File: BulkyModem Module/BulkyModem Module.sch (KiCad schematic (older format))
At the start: 12 parts, among them M1 Mounting, M2 Mounting, M3 Mounting, M4 Mounting, U1 74HCT244

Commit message: Initial layout
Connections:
- net ESP_RI: now reaches A1.23 (D5)
- no-connect marks 15 -> 14
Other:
- note added: "Note that the DCD/RI signal is shared between the two, something I'll\n"probably" get away with since they are only outgoing signals. The\n232 side will get buffered by the inverter used."
- note removed: "Note that the DCD signal is shared between the two, something I'll\n"probably" get away with since they are only outgoing signals. The\n232 side will get buffered by the inverter used."
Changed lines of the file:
@@
 NoConn ~ 8650 3825
 NoConn ~ 8650 3725
-NoConn ~ 8650 3625
 NoConn ~ 8650 3225
 NoConn ~ 8650 2925
@@
 	8650 3125 8875 3125
 $Sheet
-S 1925 1800 1025 700
+S 1925 1575 1025 825
 U 6379233A
 F0 "RS-232" 50
 F1 "rs232.sch" 50
-F2 "232_TX" I L 1925 2000 50
-F3 "232_RX" O L 1925 2100 50
-F4 "232_CTS" O L 1925 2300 50
-F5 "232_RTS" I L 1925 2200 50
-F6 "232_DCD" I L 1925 2400 50
+F2 "232_TX" I L 1925 1775 50
+F3 "232_RX" O L 1925 1875 50
+F4 "232_CTS" O L 1925 2075 50
+F5 "232_RTS" I L 1925 1975 50
+F6 "232_DCD" I L 1925 2175 50
+F7 "232_RI" I L 1925 2275 50
 $EndSheet
 $Sheet
@@
 	2425 3600 2500 3600
 Wire Wire Line
-	1925 2000 1400 2000
-Wire Wire Line
-	1400 2100 1925 2100
-Wire Wire Line
-	1925 2200 1400 2200
-Wire Wire Line
-	1400 2300 1925 2300
-Text Label 1425 2000 0    50   ~ 0
+	1925 1775 1400 1775
+Wire Wire Line
+	1400 1875 1925 1875
+Wire Wire Line
+	1925 1975 1400 1975
+Wire Wire Line
+	1400 2075 1925 2075
+Text Label 1425 1775 0    50   ~ 0
 232_TX
-Text Label 1425 2100 0    50   ~ 0
+Text Label 1425 1875 0    50   ~ 0
 232_RX
-Text Label 1425 2200 0    50   ~ 0
+Text Label 1425 1975 0    50   ~ 0
 232_RTS
-Text Label 1425 2300 0    50   ~ 0
+Text Label 1425 2075 0    50   ~ 0
 232_CTS
 Entry Wire Line
-	1400 2000 1300 2100
-Entry Wire Line
-	1400 2100 1300 2200
-Entry Wire Line
-	1400 2200 1300 2300
-Entry Wire Line
-	1400 2300 1300 2400
+	1400 1775 1300 1875
+Entry Wire Line
+	1400 1875 1300 1975
+Entry Wire Line
+	1400 1975 1300 2075
+Entry Wire Line
+	1400 2075 1300 2175
 Text Label 4000 3600 2    50   ~ 0
 232_TX
@@
 	4700 3900 4600 4000
 $Sheet
-S 3050 1800 1025 700
+S 3050 1575 1025 825
 U 63AD1846
 F0 "C64 UserPort" 50
 F1 "c64_userport.sch" 50
-F2 "C64_CTS" O R 4075 2300 50
-F3 "C64_RX" O R 4075 2100 50
-F4 "C64_TX" I R 4075 2000 50
-F5 "C64_RTS" I R 4075 2200 50
-F6 "C64_DCD" I R 4075 2400 50
+F2 "C64_CTS" O R 4075 2075 50
+F3 "C64_RX" O R 4075 1875 50
+F4 "C64_TX" I R 4075 1775 50
+F5 "C64_RTS" I R 4075 1975 50
+F6 "C64_DCD" I R 4075 2175 50
+F7 "C64_RI" I R 4075 2275 50
 $EndSheet
 Wire Wire Line
-	4075 2000 4600 2000
-Wire Wire Line
-	4600 2100 4075 2100
-Wire Wire Line
-	4075 2200 4600 2200
-Wire Wire Line
-	4600 2300 4075 2300
-Text Label 4575 2000 2    50   ~ 0
+	4075 1775 4600 1775
+Wire Wire Line
+	4600 1875 4075 1875
+Wire Wire Line
+	4075 1975 4600 1975
+Wire Wire Line
+	4600 2075 4075 2075
+Text Label 4575 1775 2    50   ~ 0
 C64_TX
-Text Label 4575 2100 2    50   ~ 0
+Text Label 4575 1875 2    50   ~ 0
 C64_RX
-Text Label 4575 2200 2    50   ~ 0
+Text Label 4575 1975 2    50   ~ 0
 C64_RTS
-Text Label 4575 2300 2    50   ~ 0
+Text Label 4575 2075 2    50   ~ 0
 C64_CTS
 Entry Wire Line
-	4600 2000 4700 2100
-Entry Wire Line
-	4600 2100 4700 2200
-Entry Wire Line
-	4600 2200 4700 2300
-Entry Wire Line
-	4600 2300 4700 2400
+	4600 1775 4700 1875
+Entry Wire Line
+	4600 1875 4700 1975
+Entry Wire Line
+	4600 1975 4700 2075
+Entry Wire Line
+	4600 2075 4700 2175
 $Sheet
 S 1925 6225 1025 700
@@
 Wire Wire Line
 	8650 3325 8875 3325
-Text GLabel 1850 2400 0    50   Input ~ 0
+Text GLabel 1850 2175 0    50   Input ~ 0
 ESP_DCD
 Wire Wire Line
-	1850 2400 1925 2400
-Text GLabel 4150 2400 2    50   Input ~ 0
+	1850 2175 1925 2175
+Text GLabel 4150 2175 2    50   Input ~ 0
 ESP_DCD
 Wire Wire Line
-	4150 2400 4075 2400
+	4150 2175 4075 2175
 Text Notes 1725 2900 0    50   ~ 0
-Note that the DCD signal is shared between the two, something I'll\n"probably" get away with since they are only outgoing signals. The\n232 side will get buffered by the inverter used.
+Note that the DCD/RI signal is shared between the two, something I'll\n"probably" get away with since they are only outgoing signals. The\n232 side will get buffered by the inverter used.
+Text GLabel 1850 2275 0    50   Input ~ 0
+ESP_RI
+Wire Wire Line
+	1850 2275 1925 2275
+Text GLabel 4150 2275 2    50   Input ~ 0
+ESP_RI
+Wire Wire Line
+	4150 2275 4075 2275
+Text GLabel 8875 3625 2    50   Output ~ 0
+ESP_RI
+Wire Wire Line
+	8650 3625 8875 3625
 Wire Bus Line
 	4700 1425 4700 4000

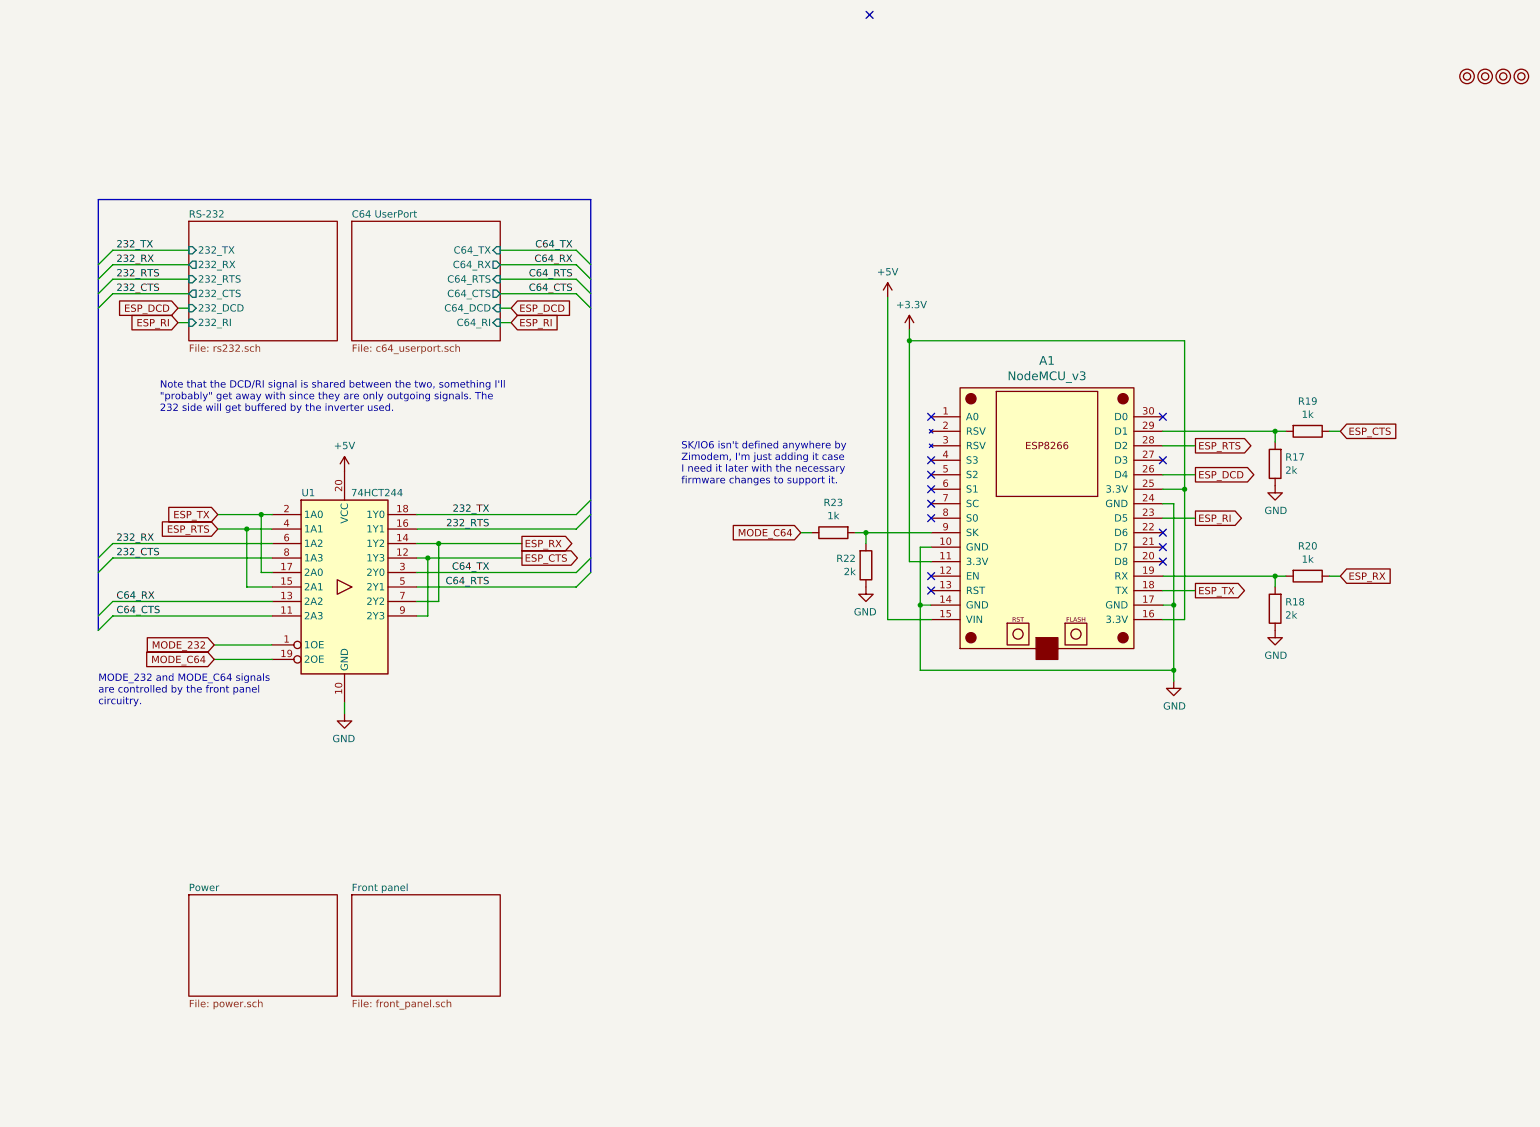
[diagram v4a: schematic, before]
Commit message: Buffer RI and DCD with spare gates
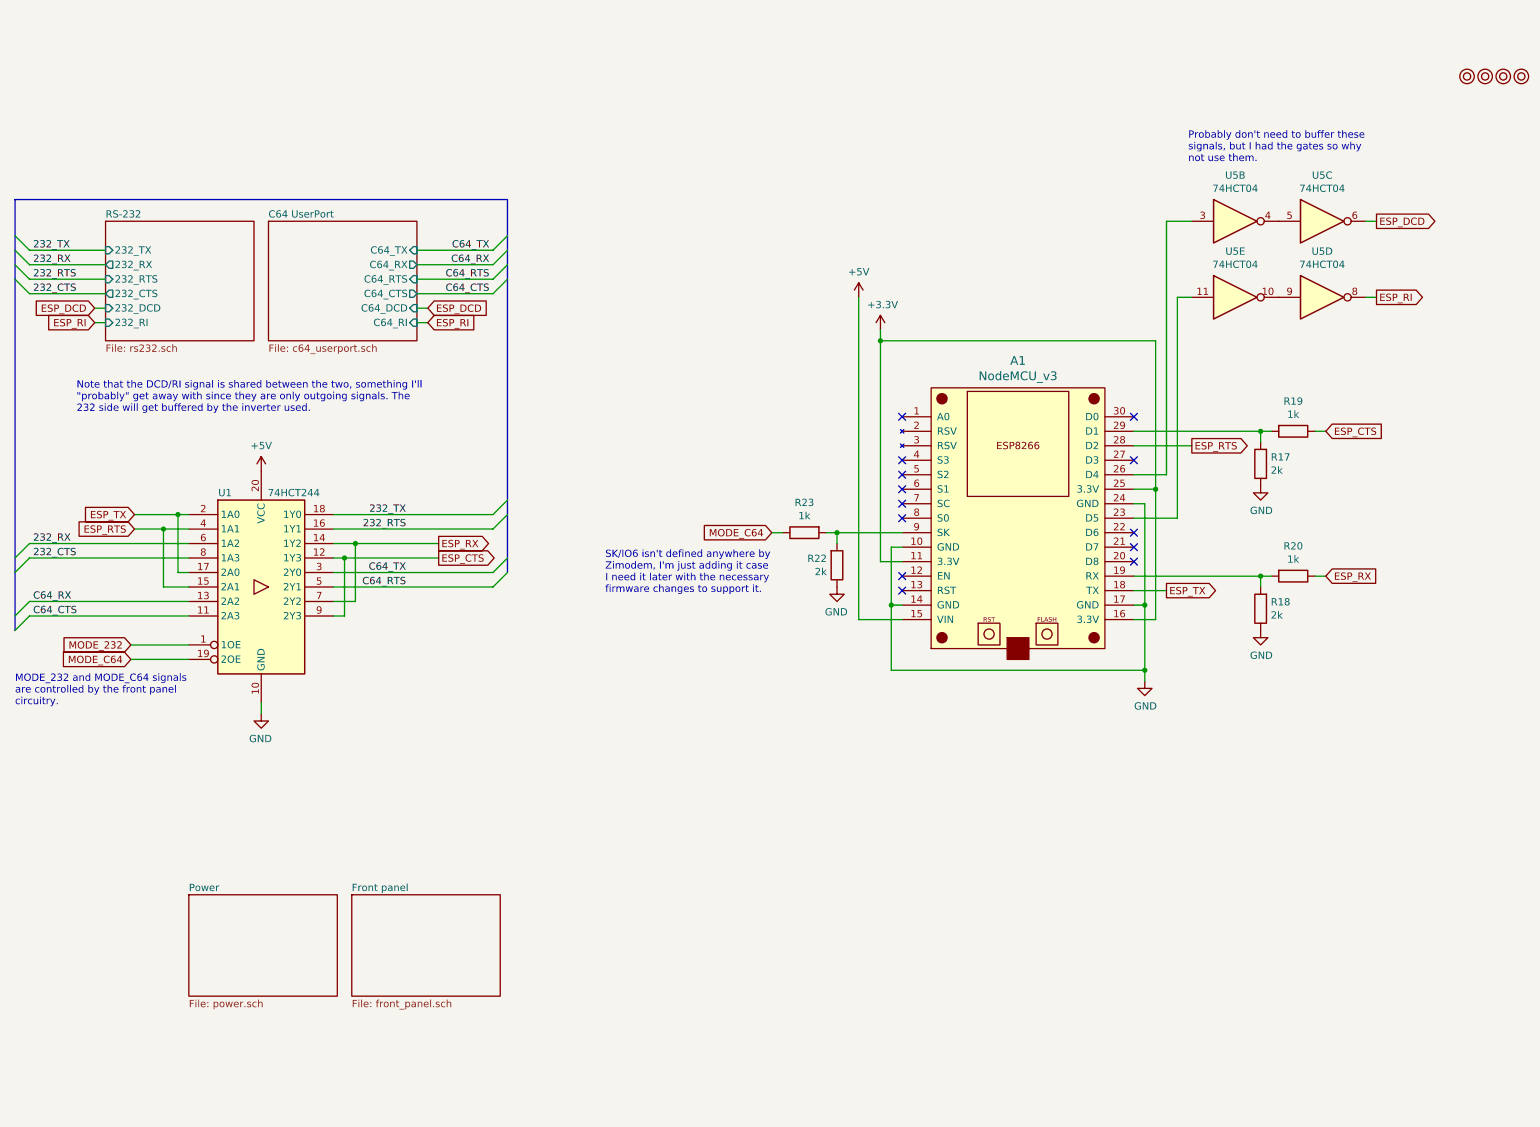
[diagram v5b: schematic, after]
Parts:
- added U5: 74HCT04, Package_DIP:DIP-14_W7.62mm_Socket_LongPads, symbol 74xx:74HCT04
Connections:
- net ESP_DCD: now also U5.6; no longer A1.26 (D4)
- net ESP_RI: now also U5.8; no longer A1.23 (D5)
- new net: A1.26 (D4), U5.3
- new net: U5.4, U5.5
- new net: U5.10, U5.9
- new net: A1.23 (D5), U5.11
- no-connect marks 14 -> 13
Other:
- note added: "Probably don't need to buffer these\nsignals, but I had the gates so why\nnot use them."
- moved on the sheet: A1, R17, R18, R19, R20, R22, R23, U1

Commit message: Tweak schematic in order to fix LEDs and default jumper settings moved to working configuration
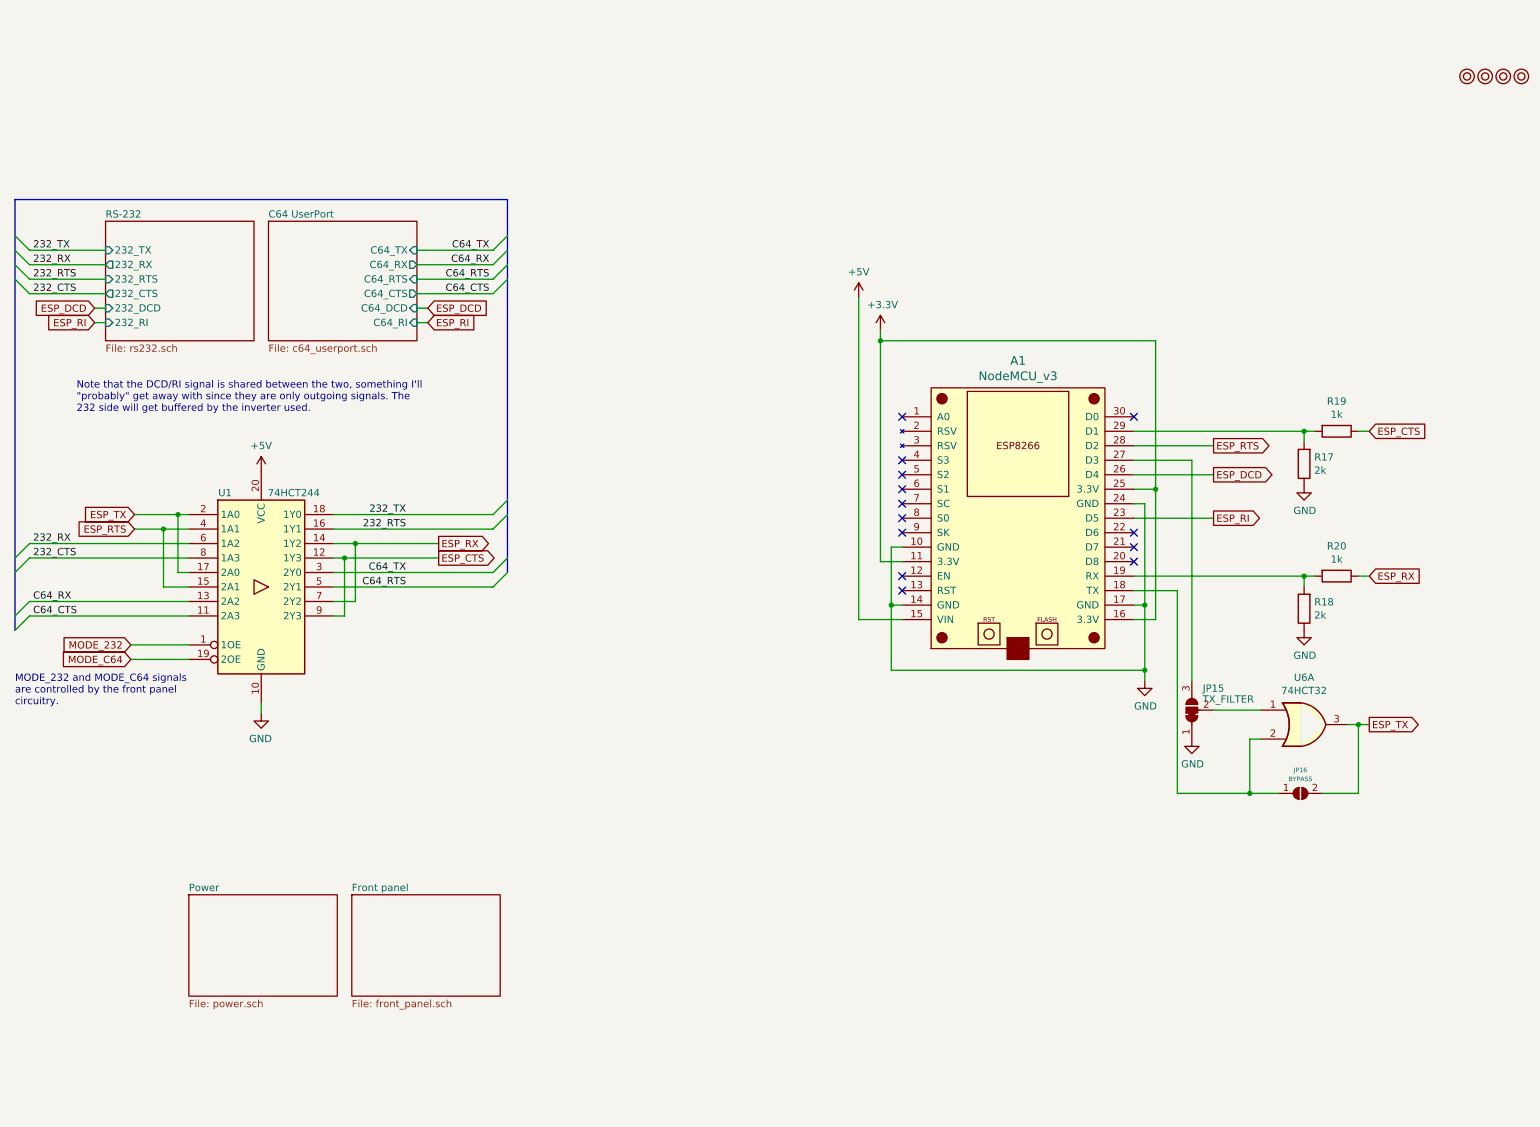
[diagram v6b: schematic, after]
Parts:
- removed R22: 2k, resistor:R_Axial_DIN0207_L6.3mm_D2.5mm_P10.16mm_Horizontal, symbol Device:R
- removed R23: 1k, resistor:R_Axial_DIN0207_L6.3mm_D2.5mm_P10.16mm_Horizontal, symbol Device:R
- removed U5: 74HCT04, Package_DIP:DIP-14_W7.62mm_Socket_LongPads, symbol 74xx:74HCT04
- added JP15: TX_FILTER, Jumper:SolderJumper-3_P1.3mm_Open_RoundedPad1.0x1.5mm, symbol BulkyModem:Swap_Output
- added JP16: BYPASS, Jumper:SolderJumper-2_P1.3mm_Open_Pad1.0x1.5mm, symbol Jumper:SolderJumper_2_Open
- added U6: 74HCT32, symbol 74xx:74LS32
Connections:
- net ESP_DCD: now also A1.26 (D4)
- net ESP_RI: now also A1.23 (D5)
- net ESP_TX: now also JP16.2 (B), U6.3; no longer A1.18 (TX)
- net GND: now also JP15.1 (A)
- net at A1.27 (D3): now also JP15.3 (B)
- new net: A1.18 (TX), JP16.1 (A), U6.2
- new net: JP15.2 (C), U6.1
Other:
- note removed: "Probably don't need to buffer these\nsignals, but I had the gates so why\nnot use them."
- note removed: "SK/IO6 isn't defined anywhere by\nZimodem, I'm just adding it case\nI need it later with the necessary\nfirmware changes to support it."
- moved on the sheet: R17, R18, R19, R20
